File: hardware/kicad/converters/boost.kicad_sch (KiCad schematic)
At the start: 5 parts, among them M1 IRF540N

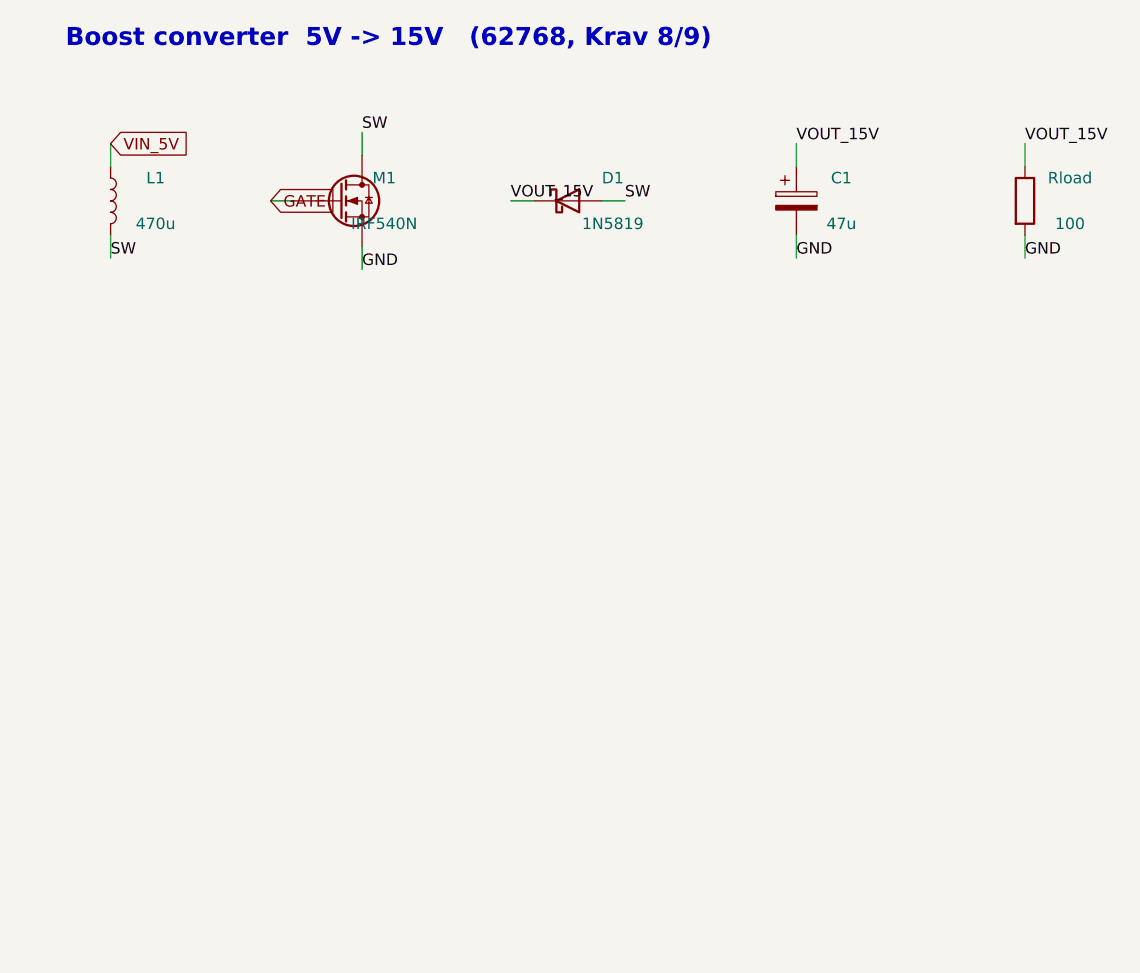
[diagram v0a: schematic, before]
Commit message: Add isolated optocoupler gate drive to buck & boost converters
- 4N25 opto isolates Arduino PWM from the power stage (non-inverting)
- boost (low-side): gate pulldown to GND, +12V supply
- buck rebuilt in wired style with high-side switch: pulldown to SW,
  floating +12V_SW (gate referenced to the MOSFET source)
- new helpers: buck_build.py, add_optocoupler.py; README documents the
  drive and the 4N25 drive-strength caveat (needs a BJT buffer at 50 kHz)
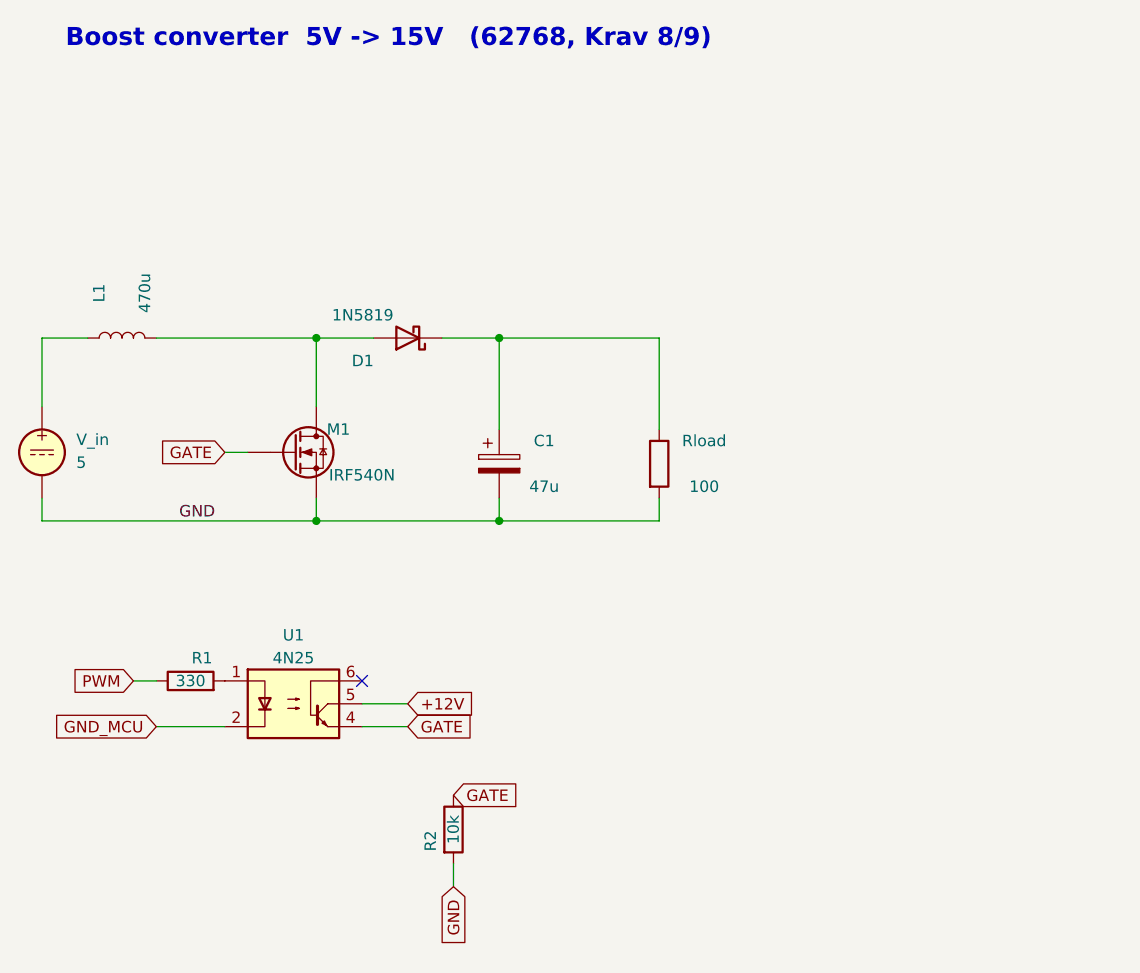
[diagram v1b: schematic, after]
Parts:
- added R1: 330, symbol Device:R
- added R2: 10k, symbol Device:R
- added U1: 4N25, symbol Isolator:4N25
- added V_in: 5, symbol Simulation_SPICE:VDC
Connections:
- net GATE: now also R2.1, U1.4
- net GND: now also R2.2, V_in.2
- net SW: no longer names the net of D1.2 (A), L1.2, M1.D
- net VIN_5V: no longer names the net of L1.1
- net VIN_5V: now also V_in.1
- net VOUT_15V: no longer names the net of C1.1, D1.1 (K), Rload.1
- new net: R1.2, U1.1
- new net +12V: U1.5
- new net GND_MCU: U1.2
- new net PWM: R1.1
- no-connect marks 0 -> 1
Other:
- moved on the sheet: C1, D1, L1, M1, Rload

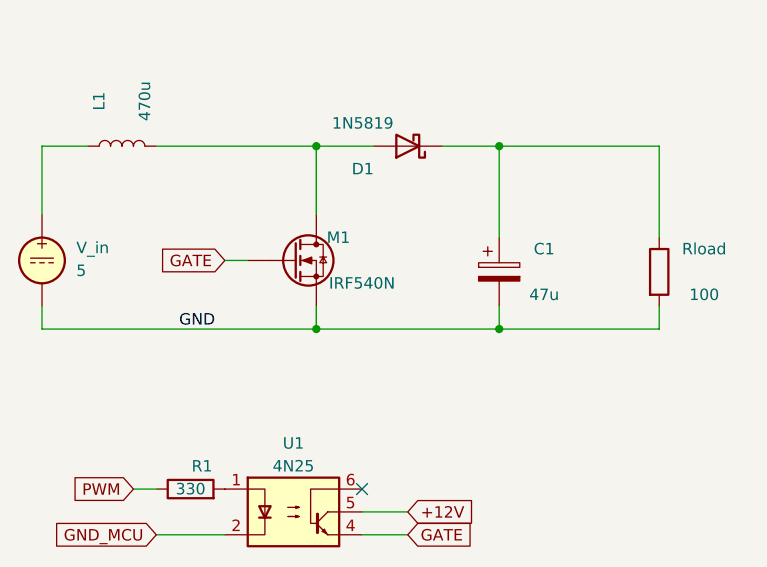
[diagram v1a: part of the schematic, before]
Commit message: Switch MOSFET from IRF540N to IRF530N + add datasheet VDMOS model
- IRF530N is a better fit at low current / 10 kHz: half the gate charge
  (~34 nC) is much easier for the 4N25 optocoupler to drive
- updated schematics, generators, LTspice scripts, READMEs, BOM/docs
- added models/IRF530N.lib: ngspice VDMOS model parameterised from the
  IRF530N datasheet (Rds(on) 90 mOhm, Vth ~3.5 V, Qg 34 nC, body diode)
  for loading into the KiCad simulator
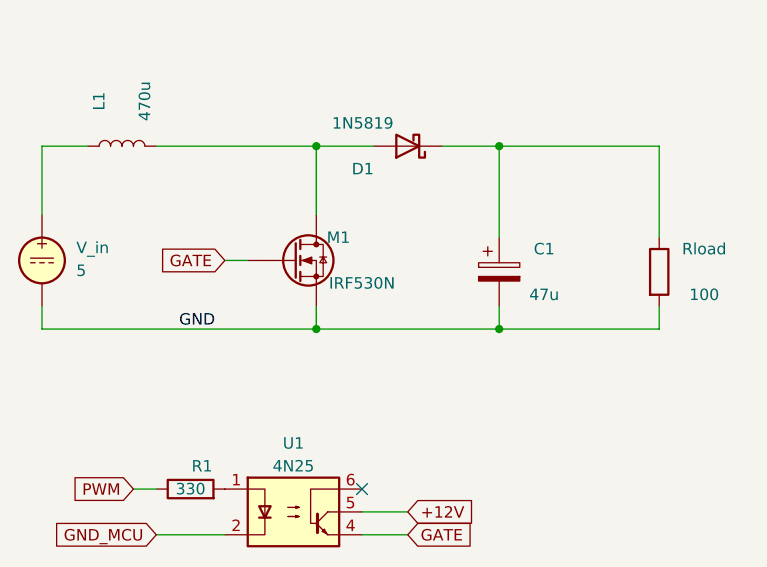
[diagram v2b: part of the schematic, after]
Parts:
- M1: value IRF540N -> IRF530N
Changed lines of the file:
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@@
 			)
 		)
-		(property "Value" "IRF540N"
+		(property "Value" "IRF530N"
 			(at 116.84 119.38 0)
 			(effects
